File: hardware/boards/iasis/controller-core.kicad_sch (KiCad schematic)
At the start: 39 parts, among them J1101 SWD debug, SW1101 B3U-1000P, SW1102 B3U-1000P, U1101 RP2354B, Y1101 ABM8-272-T3

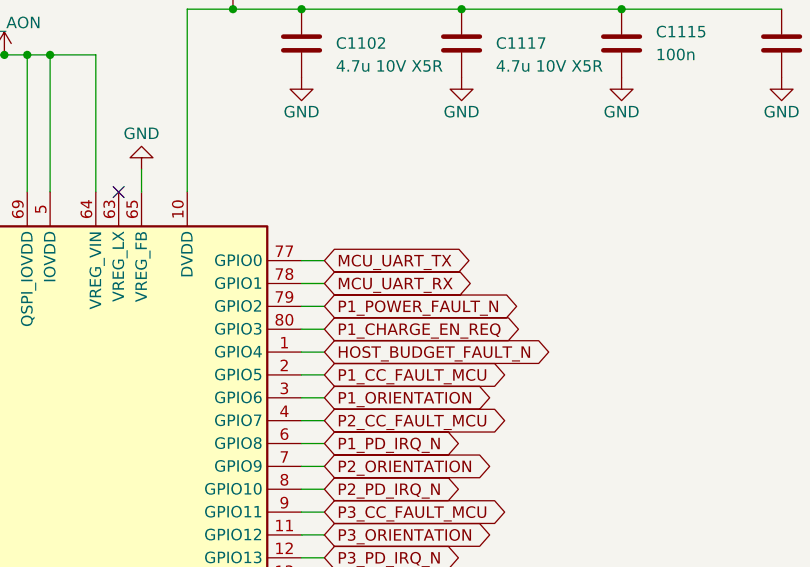
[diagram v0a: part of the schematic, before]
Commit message: feat(hardware): add independent mux reset
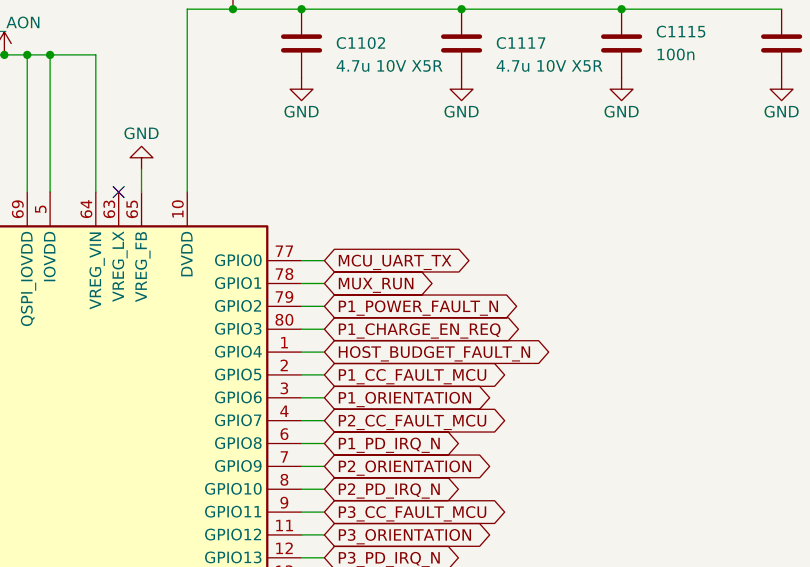
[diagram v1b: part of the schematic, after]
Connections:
- net MCU_UART_RX renamed MUX_RUN
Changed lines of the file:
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@@
 		)
 	)
-	(global_label "MCU_UART_RX"
+	(global_label "MUX_RUN"
 		(shape bidirectional)
 		(at 231.14 106.68 0)
